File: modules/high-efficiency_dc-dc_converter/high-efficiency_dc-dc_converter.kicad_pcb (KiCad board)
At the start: 2 copper layers, 12 parts

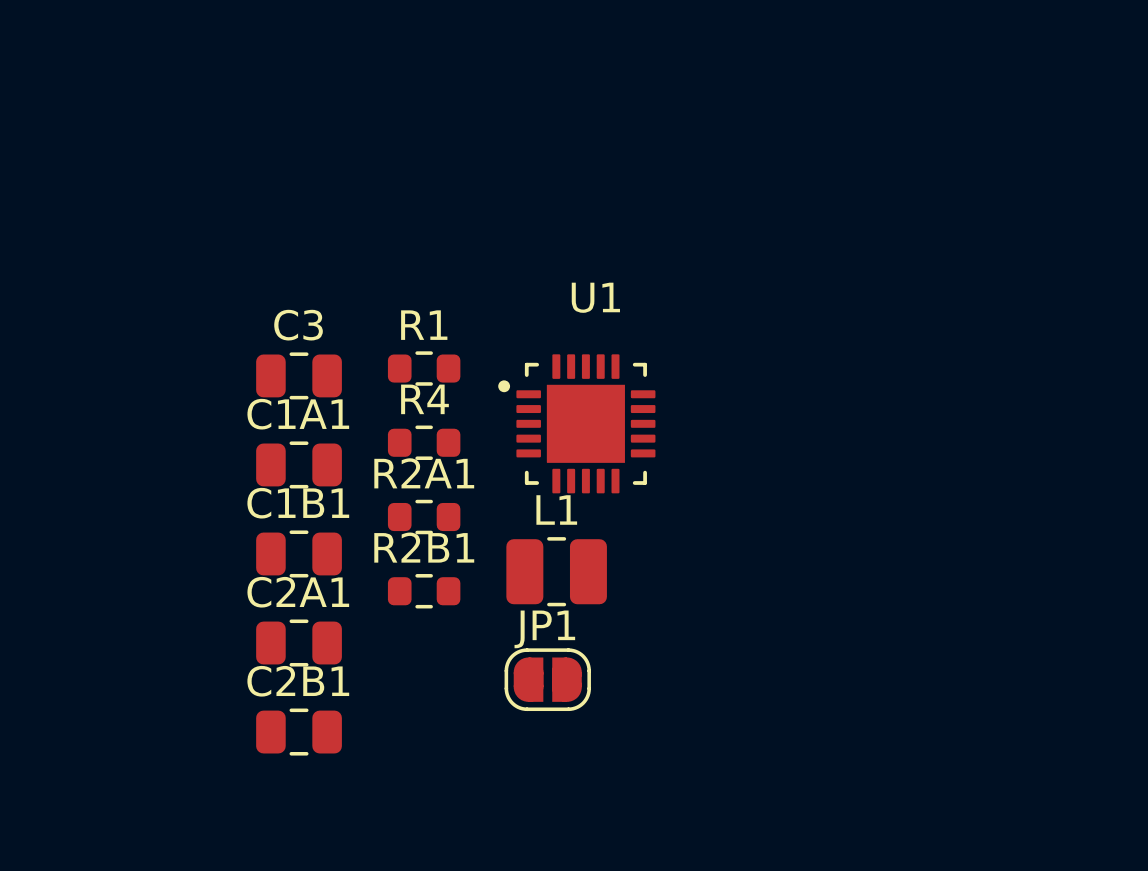
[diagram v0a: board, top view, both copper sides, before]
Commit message: update schematic, slightly compact PCB layout
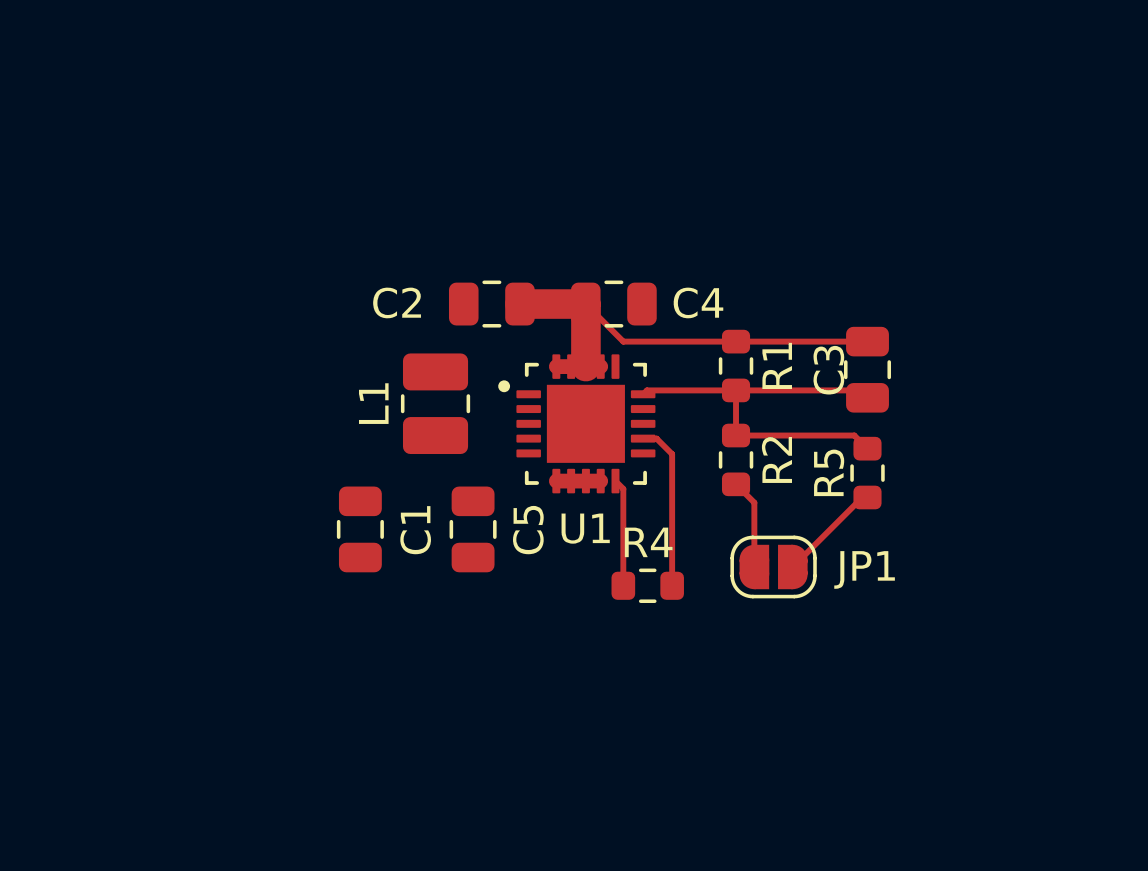
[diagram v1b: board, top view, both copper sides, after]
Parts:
- L1: value L -> 1uH
- moved C3 19.2 mm to (71.8, 38.4), turned to -90 degrees
- moved C4 18.0 mm to (63.2, 36.2)
- moved R5 15.5 mm to (71.8, 41.9), turned to -90 degrees
- moved C2 13.2 mm to (59.1, 36.2), turned to 180 degrees
- moved R2 10.7 mm to (67.3, 41.5), turned to -90 degrees
- moved R1 10.5 mm to (67.3, 38.3), turned to -90 degrees
- moved R4 8.97 mm to (64.3, 45.7)
- moved JP1 8.53 mm to (68.6, 45.1)
- moved L1 7.00 mm to (57.1, 39.6), turned to 90 degrees
- moved C5 6.28 mm to (58.4, 43.8), turned to 90 degrees
- moved C1 2.23 mm to (54.6, 43.8), turned to 90 degrees
- renumbered C1B1 to C1, C2A1 to C2, C2B1 to C4, C1A1 to C5, R2A1 to R2, R2B1 to R5
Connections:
- U1 pad 21: (no net) -> GND
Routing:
- net VCC_OUT: track 0.00 -> 15.9 mm
- net Net-(U1-FB): track 0.00 -> 13.9 mm
- net MODE: track 0.00 -> 5.65 mm
- net VBAT: track 0.00 -> 5.15 mm
- net /5V_SEL: track 0.00 -> 3.50 mm
- net GND: track 0.00 -> 3.05 mm

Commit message: add 2x11 module symbol and footprint and use for DC:DC module
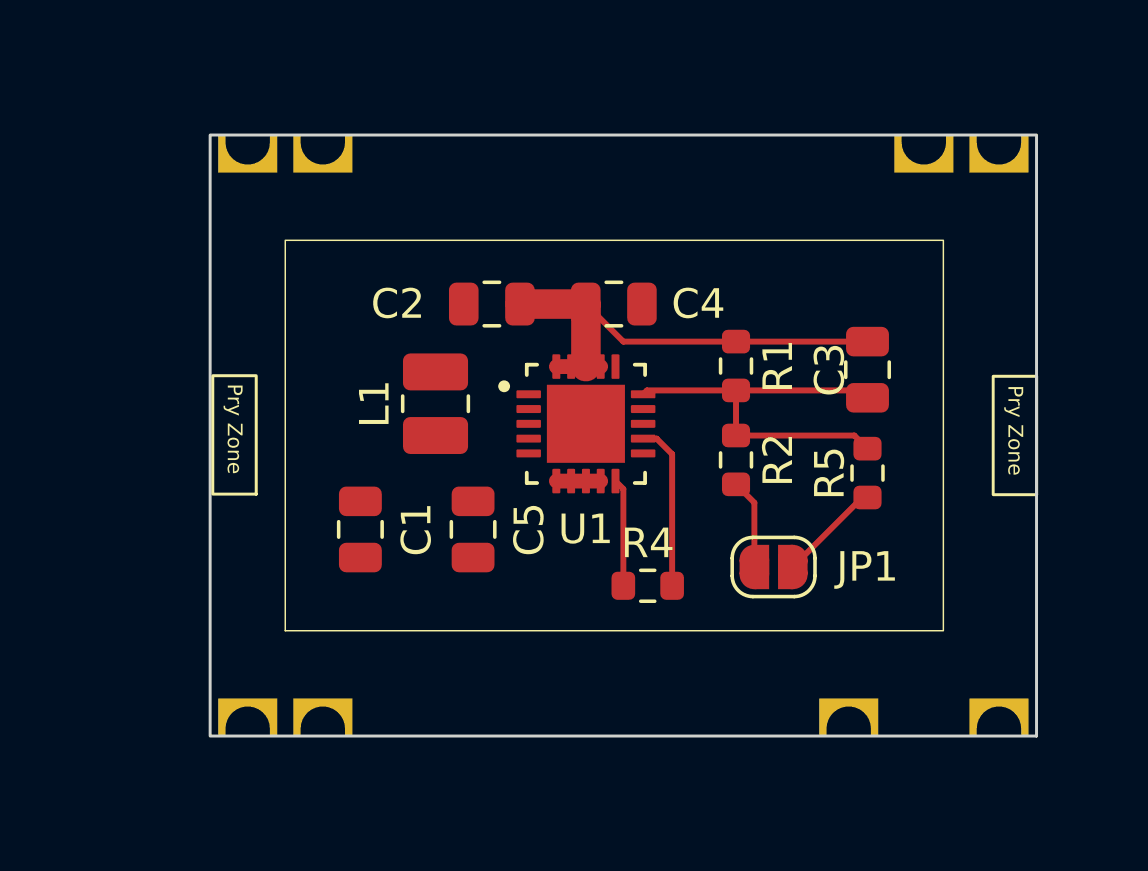
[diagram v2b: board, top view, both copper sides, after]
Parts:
- added M1: ~, MegaCastle:MegaCastle2x11Wide-Module-I13.2x22.25-KA0780C, B.Cu at (64.8, 40.6)
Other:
- board outline added: 27.9 x 20.3 mm
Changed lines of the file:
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@@
     )
   )
-  (dimension (type aligned) (layer "User.1")
-    (pts (xy 52.07 46.355) (xy 52.07 34.925))
-    (height 0)
-    (gr_text "11.4300 mm" (at 50.92 40.64 90) (layer "User.1")
-      (effects (font (size 1 1) (thickness 0.15)))
+  (footprint "MegaCastle:MegaCastle2x11Wide-Module-I13.2x22.25-KA0780C" (layer "B.Cu")
+    (at 64.77 40.64 90)
+    (property "Sheetfile" "high-efficiency_dc-dc_converter.kicad_sch")
+    (property "Sheetname" "")
+    (attr smd)
+    (fp_text reference "M1" (at -7.62 -10.16 180 unlocked) (layer "B.SilkS")
+        (effects (font (size 1 1) (thickness 0.1)) (justify mirror))
     )
-    (format (prefix "") (suffix "") (units 3) (units_format 1) (precision 4))
-    (style (thickness 0.1) (arrow_length 1.27) (text_position_mode 0) (extension_height 0.58642) (extension_offset 0.5) keep_text_aligned)
-  )
-  (dimension (type aligned) (layer "User.1")
-    (pts (xy 73.66 47.625) (xy 53.34 47.625))
-    (height 0)
-    (gr_text "20.3200 mm" (at 63.5 46.475) (layer "User.1")
-      (effects (font (size 1 1) (thickness 0.15)))
+    (fp_text value "~" (at 11.43 0 180 unlocked) (layer "B.Fab")
+        (effects (font (size 1 1) (thickness 0.15)) (justify mirror))
     )
-    (format (prefix "") (suffix "") (units 3) (units_format 1) (precision 4))
-    (style (thickness 0.1) (arrow_length 1.27) (text_position_mode 0) (extension_height 0.58642) (extension_offset 0.5) keep_text_aligned)
+    (fp_text user "Pry Zone" (at 1.705127 11.688692 270 unlocked) (layer "F.SilkS")
+        (effects (font (size 0.5 0.5) (thickness 0.1)) (justify left bottom))
+    )
+    (fp_text user "Pry Zone" (at 1.755819 -14.704296 270 unlocked) (layer "F.SilkS")
+        (effects (font (size 0.5 0.5) (thickness 0.1)) (justify left bottom))
+    )
+    (fp_text user "${REFERENCE}" (at -7.62 6.35 180 unlocked) (layer "B.Fab")
+        (effects (font (size 1 1) (thickness 0.15)) (justify mirror))
+    )
+    (fp_rect (start -6.6 -12.7) (end 6.6 9.55)
+      (stroke (width 0.05) (type default)) (fill none) (layer "F.SilkS"))
+    (fp_rect (start -2.000193 12.704102) (end 2.003564 11.23551)
+      (stroke (width 0.1) (type default)) (fill none) (layer "F.SilkS"))
+    (fp_rect (start -1.981655 -13.68174) (end 2.022102 -15.150332)
+      (stroke (width 0.1) (type default)) (fill none) (layer "F.SilkS"))
+    (fp_rect (start -10.16 12.7) (end 10.16 -15.24)
+      (stroke (width 0.1) (type default)) (fill none) (layer "Edge.Cuts"))
+    (dimension (type aligned) (layer "Dwgs.User")
+      (pts (xy 74.32 47.24) (xy 74.32 34.04))
+      (height 4.42)
+      (gr_text "13.2000 mm" (at 77.59 40.64 90) (layer "Dwgs.User")
+        (effects (font (size 1 1) (thickness 0.15)))
+      )
+      (format (prefix "") (suffix "") (units 3) (units_format 1) (precision 4))
+      (style (thickness 0.1) (arrow_length 1.27) (text_position_mode 0) (extension_height 0.58642) (extension_offset 0.5) keep_text_aligned)
+    )
+    (dimension (type aligned) (layer "Dwgs.User")
+      (pts (xy 74.32 34.04) (xy 52.07 34.04))
+      (height 9.91)
+      (gr_text "22.2500 mm" (at 63.195 22.98) (layer "Dwgs.User")
+        (effects (font (size 1 1) (thickness 0.15)))
+      )
+      (format (prefix "") (suffix "") (units 3) (units_format 1) (precision 4))
+      (style (thickness 0.1) (arrow_length 1.27) (text_position_mode 0) (extension_height 0.58642) (extension_offset 0.5) keep_text_aligned)
+    )
+    (pad "1" thru_hole rect (at -10.16 11.43 90) (size 1.27 2) (drill oval 2 1.5 (offset 0.635 0)) (property pad_prop_castellated) (layers "*.Cu" "*.Mask")
+      (net 1 "VBAT") (pinfunction "VCC") (pintype "bidirectional") (thermal_bridge_angle 45))
+    (pad "3" thru_hole rect (at -10.16 6.35 90) (size 1.27 2) (drill oval 2 1.5 (offset 0.635 0)) (property pad_prop_castellated) (layers "*.Cu" "*.Mask")
+      (net 5 "{slash}5V_SEL") (pintype "bidirectional") (thermal_bridge_angle 45))
+    (pad "10" thru_hole rect (at -10.16 -11.43 90) (size 1.27 2) (drill oval 2 1.5 (offset 0.635 0)) (property pad_prop_castellated) (layers "*.Cu" "*.Mask")
+      (net 3 "VCC_OUT") (pintype "bidirectional") (thermal_bridge_angle 45))
+    (pad "11" thru_hole rect (at -10.16 -13.97 90) (size 1.27 2) (drill oval 2 1.5 (offset 0.635 0)) (property pad_prop_castellated) (layers "*.Cu" "*.Mask")
+      (net 2 "GND") (pinfunction "GND") (pintype "bidirectional") (thermal_bridge_angle 45))
+    (pad "12" thru_hole rect (at 10.16 11.43 90) (size 1.27 2) (drill oval 2 1.5 (offset -0.635 0)) (property pad_prop_castellated) (layers "*.Cu" "*.Mask")
+      (net 3 "VCC_OUT") (pintype "bidirectional") (thermal_bridge_angle 45))
+    (pad "13" thru_hole rect (at 10.16 8.89 90) (size 1.27 2) (drill oval 2 1.5 (offset -0.635 0)) (property pad_prop_castellated) (layers "*.Cu" "*.Mask")
+      (net 10 "EN") (pintype "bidirectional") (thermal_bridge_angle 45))
+    (pad "21" thru_hole rect (at 10.16 -11.43 90) (size 1.27 2) (drill oval 2 1.5 (offset -0.635 0)) (property pad_prop_castellated) (layers "*.Cu" "*.Mask")
+      (net 8 "MODE") (pintype "bidirectional") (thermal_bridge_angle 45))
+    (pad "22" thru_hole rect (at 10.16 -13.97 90) (size 1.27 2) (drill oval 2 1.5 (offset -0.635 0)) (property pad_prop_castellated) (layers "*.Cu" "*.Mask")
+      (net 3 "VCC_OUT") (pintype "bidirectional") (thermal_bridge_angle 45))
+    (zone (net 0) (net_name "") (layer "F.Cu") (name "Upper Pry Zone") (hatch edge 0.5)
+      (connect_pads (clearance 0))
+      (min_thickness 0.25) (filled_areas_thickness no)
+      (keepout (tracks not_allowed) (vias not_allowed) (pads not_allowed) (copperpour allowed) (footprints not_allowed))
+      (fill (thermal_gap 0.5) (thermal_bridge_width 0.5))
+      (polygon
+        (pts
+          (xy 49.336879 42.637947)
+          (xy 50.8 42.641365)
+          (xy 50.794165 38.635336)
+          (xy 49.333778 38.647642)
+        )
+      )
+    )
+    (zone (net 0) (net_name "") (layer "F.Cu") (hatch edge 0.5)
+      (connect_pads (clearance 0))
+      (min_thickness 0.25) (filled_areas_thickness no)
+      (keepout (tracks allowed) (vias allowed) (pads allowed) (copperpour allowed) (footprints not_allowed))
+      (fill (thermal_gap 0.5) (thermal_bridge_width 0.5))
+      (polygon
+        (pts
+          (xy 52.34 50.8)
+          (xy 74.526616 50.535831)
+          (xy 74.526386 48.8)
+          (xy 52.34 48.8)
+        )
+      )
+    )
+    (zone (net 0) (net_name "") (layer "F.Cu") (hatch edge 0.5)
+      (connect_pads (clearance 0))
+      (min_thickness 0.25) (filled_areas_thickness no)
+      (keepout (tracks allowed) (vias allowed) (pads allowed) (copperpour allowed) (footprints not_allowed))
+      (fill (thermal_gap 0.5) (thermal_bridge_width 0.5))
+      (polygon
+        (pts
+          (xy 52.473384 32.744169)
+          (xy 74.66 32.48)
+          (xy 74.65977 30.744169)
+          (xy 52.473384 30.744169)
+        )
+      )
+    )
+    (zone (net 0) (net_name "") (layer "F.Cu") (hatch edge 0.5)
+      (connect_pads (clearance 0))
+      (min_thickness 0.25) (filled_areas_thickness no)
+      (keepout (tracks allowed) (vias allowed) (pads allowed) (copperpour allowed) (footprints not_allowed))
+      (fill (thermal_gap 0.5) (thermal_bridge_width 0.5))
+      (polygon
+        (pts
+          (xy 57.545782 30.450109)
+          (xy 64.344682 30.418211)
+          (xy 64.357945 32.14429)
+          (xy 57.535608 32.154434)
+        )
+      )
+    )
+    (zone (net 0) (net_name "") (layer "F.Cu") (hatch edge 0.5)
+      (connect_pads (clearance 0))
+      (min_thickness 0.25) (filled_areas_thickness no)
+      (keepout (tracks allowed) (vias allowed) (pads allowed) (copperpour allowed) (footprints not_allowed))
+      (fill (thermal_gap 0.5) (thermal_bridge_width 0.5))
+      (polygon
+        (pts
+          (xy 70.245782 30.450109)
+          (xy 77.044682 30.418211)
+          (xy 77.057945 32.14429)
+          (xy 70.235608 32.154434)
+        )
+      )
+    )
+    (zone (net 0) (net_name "") (layer "F.Cu") (name "Upper Pry Zone") (hatch edge 0.5)
+      (connect_pads (clearance 0))
+      (min_thickness 0.25) (filled_areas_thickness no)
+      (keepout (tracks not_allowed) (vias not_allowed) (pads not_allowed) (copperpour allowed) (footprints not_allowed))
+      (fill (thermal_gap 0.5) (thermal_bridge_width 0.5))
+      (polygon
+        (pts
+          (xy 76.023398 42.673201)
+          (xy 77.486519 42.676619)
+          (xy 77.480684 38.67059)
+          (xy 76.020297 38.682896)
+        )
+      )
+    )
+    (zone (net 0) (net_name "") (layer "F.Cu") (hatch edge 0.5)
+      (connect_pads (clearance 0))
+      (min_thickness 0.25) (filled_areas_thickness no)
+      (keepout (tracks allowed) (vias allowed) (pads allowed) (copperpour allowed) (footprints not_allowed))
+      (fill (thermal_gap 0.5) (thermal_bridge_width 0.5))
+      (polygon
+        (pts
+          (xy 49.327377 50.552935)
+          (xy 52.285366 50.539102)
+          (xy 52.259533 30.751322)
+          (xy 49.313575 30.734093)
+          (xy 49.342714 38.638754)
+          (xy 50.803101 38.65106)
+          (xy 50.8 42.641365)
+          (xy 49.336879 42.644783)
+        )
+      )
+    )
+    (zone (net 0) (net_name "") (layer "F.Cu") (hatch edge 0.5)
+      (connect_pads (clearance 0))
+      (min_thickness 0.25) (filled_areas_thickness no)
+      (keepout (tracks allowed) (vias allowed) (pads allowed) (copperpour allowed) (footprints not_allowed))
+      (fill (thermal_gap 0.5) (thermal_bridge_width 0.5))
+      (polygon
+        (pts
+          (xy 77.484605 50.549664)
+          (xy 74.526616 50.535831)
+          (xy 74.552449 30.748051)
+          (xy 77.498407 30.730822)
+          (xy 77.469268 38.635483)
+          (xy 76.008881 38.647789)
+          (xy 76.011982 42.638094)
+          (xy 77.475103 42.641512)
+        )
+      )
+    )
   )
   (segment (start 62.735 42.18) (end 61.235 42.18) (width 0.5) (layer "F.Cu") (net 1))

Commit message: rearrange pins etc to keep to 2-layer for DC:DC module
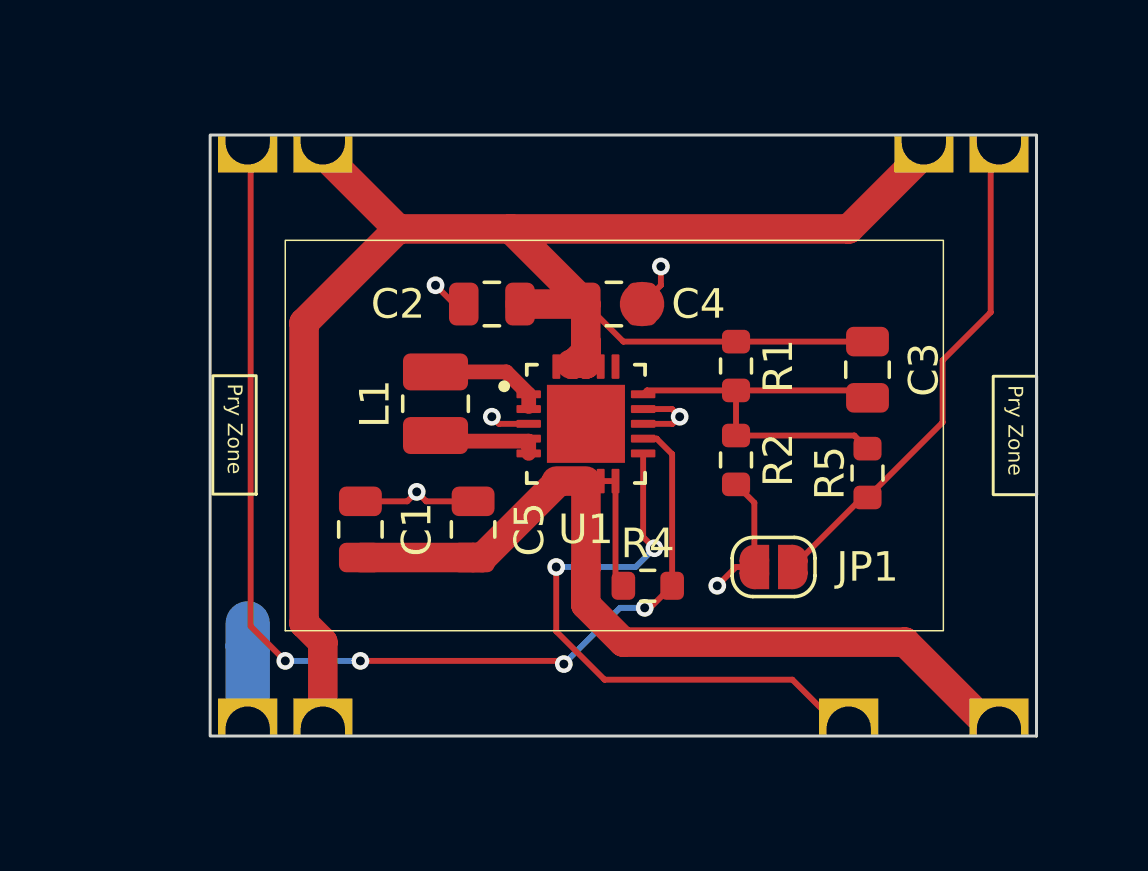
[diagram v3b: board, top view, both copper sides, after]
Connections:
- M1 pad 12: VCC_OUT -> /5V_SEL
- M1 pad 13: EN -> VCC_OUT
- M1 pad 21: MODE -> VCC_OUT
- M1 pad 22: VCC_OUT -> MODE
- M1 pad 3: /5V_SEL -> EN
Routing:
- net VCC_OUT: track 15.9 -> 60.1 mm
- net MODE: track 5.65 -> 38.4 mm, vias 0 -> 4
- net VBAT: track 5.15 -> 32.9 mm
- net EN: track 0.00 -> 20.5 mm, vias 0 -> 2
- net GND: track 3.05 -> 19.2 mm, vias 0 -> 6
- net /5V_SEL: track 3.50 -> 17.6 mm
- net Net-(L1-Pad2): track 0.00 -> 3.88 mm
- net Net-(L1-Pad1): track 0.00 -> 3.64 mm
- added copper zone on B.Cu, net GND

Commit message: add silkscreen hints etc to 2A DC:DC Module
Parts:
- moved JP1 3.83 mm to (72.4, 45.1)
- moved C3 0.63 mm to (71.1, 38.4)
- moved R1 0.63 mm to (67.9, 38.3)
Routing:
- net MODE: track 38.4 -> 40.2 mm
- net /5V_SEL: track 17.6 -> 19.0 mm
- net GND: track 19.2 -> 19.8 mm, vias 6 -> 18
- added copper zone on F.Cu, net GND
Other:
- board text added: "/5V SEL"
- board text added: "MEGAphone 2A DC:DC Module"
- board text added: "U1 ISL91127IRAZ"
- board text added: "github.com/gardners/"
- board text added: "megaphone-r5-modular"
- board text added: "r20250209"
